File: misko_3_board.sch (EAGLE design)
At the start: 179 parts, among them IC1 ATMEGA1281-16AU, IC10 ORG1510-MK4, IC11 TPS3808G33DBVT, IC12 LTC4425, IC13 RN-42, IC14 ADXL345, IC15 74HCT1G32, IC16 FM25W256-SOIC, IC17 MICROSD_SPI_MODE, IC18 FH12-30S-0.5SH, IC19 DS1394U-33+, IC2 MC1525TT, IC20 115Q-BCA0, IC21 SIM800, IC3 TMP36GRTZ, IC4 TPS63031, IC5 MCP73871-2AAI/ML, IC6 SN74HCT14DR, IC7 FT230XS, IC8 SN74LVC1G3157DBVR - BT switch, IC9 SN74LVC1G3157DBVR - GPS switch, Q1 8MHz, Q2 LFXTAL016178R, T1 BSS84

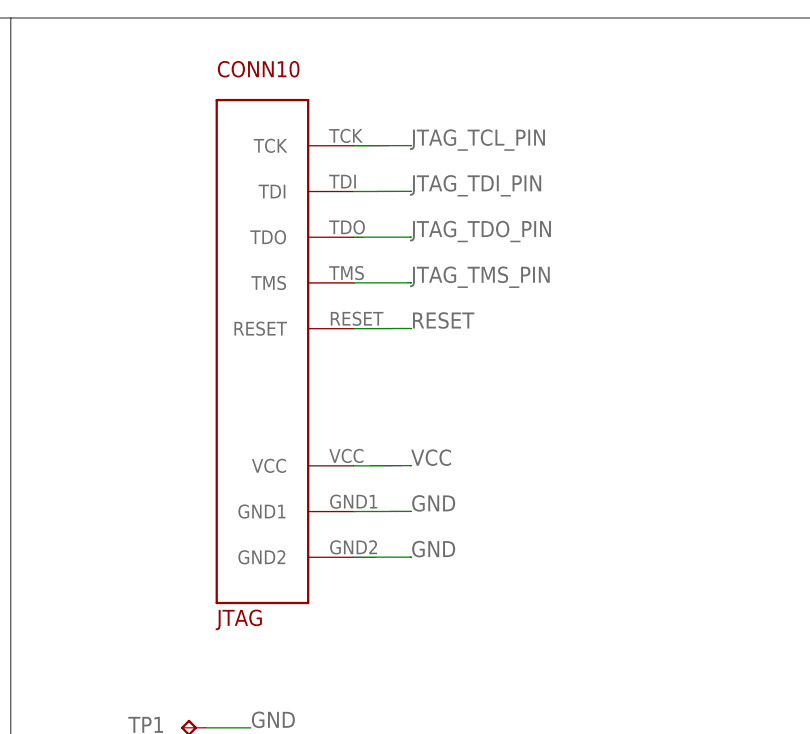
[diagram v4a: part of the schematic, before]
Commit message: - corrected for larger holes on 1.27mm connectors - moved fiducials around - rerouted a few traces around the 1.27mm connectors - added milling around mini usb socket
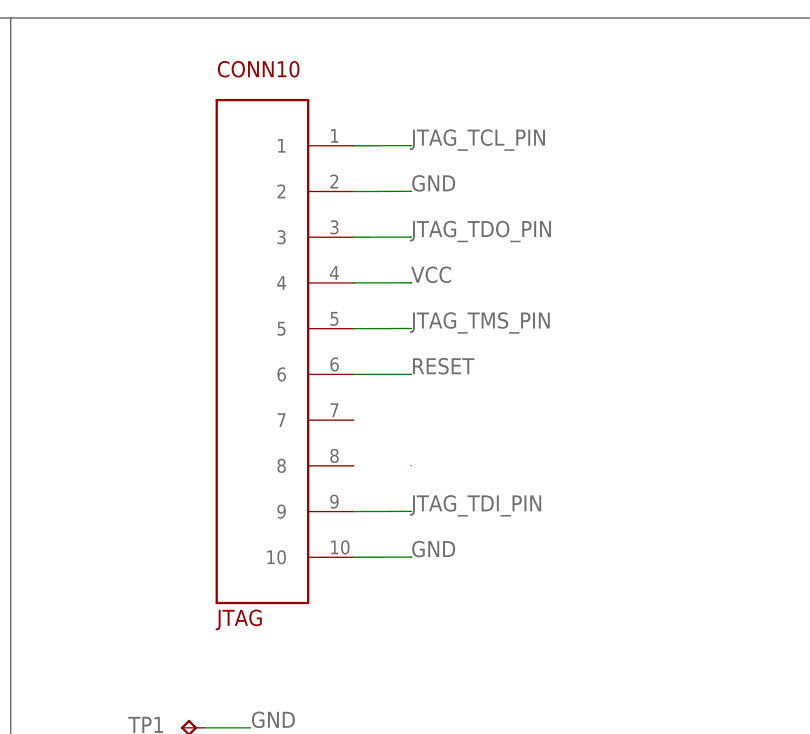
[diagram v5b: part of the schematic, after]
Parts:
- CONN10: device JTAG 1.27mm 10pin header:JTAG-1.27-10-PIN-HEADER -> 1.27mm 10pin header:1.27-10-PIN-HEADER
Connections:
- net GND: now also CONN10.10, CONN10.2; no longer CONN10.GND1, CONN10.GND2
- net JTAG_TCL_PIN: now also CONN10.1; no longer CONN10.TCK
- net JTAG_TDI_PIN: now also CONN10.9; no longer CONN10.TDI
- net JTAG_TDO_PIN: now also CONN10.3; no longer CONN10.TDO
- net JTAG_TMS_PIN: now also CONN10.5; no longer CONN10.TMS
- net RESET: now also CONN10.6; no longer CONN10.RESET
- net VCC: now also CONN10.4; no longer CONN10.VCC
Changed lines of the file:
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@@
 <setting verticaltext="up"/>
 </settings>
-<grid distance="0.1" unitdist="inch" unit="inch" style="lines" multiple="1" display="no" altdistance="0.01" altunitdist="inch" altunit="inch"/>
+<grid distance="1.27" unitdist="mm" unit="mm" style="lines" multiple="1" display="no" altdistance="0.01" altunitdist="inch" altunit="inch"/>
 <layers>
 <layer number="1" name="Top" color="4" fill="1" visible="no" active="no"/>
@@
 <part name="R54" library="rcl" deviceset="R-EU_" device="R0805" value="1k"/>
 <part name="C30" library="resistor" deviceset="C-EU" device="C0805" value="0.47µF"/>
-<part name="CONN10" library="JTAG 1.27mm 10pin header" deviceset="JTAG-1.27-10-PIN-HEADER" device="" value="JTAG"/>
+<part name="CONN10" library="1.27mm 10pin header" deviceset="1.27-10-PIN-HEADER" device="" value="JTAG"/>
 <part name="CONN12" library="1.27mm 10pin header" deviceset="1.27-10-PIN-HEADER" device="" value="board"/>
 <part name="CONN13" library="1.27mm 10pin header" deviceset="1.27-10-PIN-HEADER" device="" value="lid"/>
@@
 </segment>
 <segment>
-<pinref part="CONN10" gate="G$1" pin="VCC"/>
-<wire x1="278.13" y1="810.24" x2="284.48" y2="810.26" width="0.1524" layer="91"/>
 <wire x1="284.48" y1="810.24" x2="284.48" y2="810.26" width="0.1524" layer="91"/>
-<label x="284.48" y="810.26" size="1.778" layer="95" ratio="9"/>
 </segment>
 <segment>
@@
 <label x="213.36" y="76.2" size="1.778" layer="95"/>
 </segment>
+<segment>
+<pinref part="CONN10" gate="G$1" pin="4"/>
+<wire x1="278.13" y1="830.56" x2="284.48" y2="830.58" width="0.1524" layer="91"/>
+<wire x1="284.48" y1="830.56" x2="284.48" y2="830.58" width="0.1524" layer="91"/>
+<label x="284.48" y="830.58" size="1.778" layer="95" ratio="9"/>
+</segment>
 </net>
 <net name="GND" class="0">
@@
 </segment>
 <segment>
-<pinref part="CONN10" gate="G$1" pin="GND1"/>
-<wire x1="278.13" y1="805.16" x2="284.48" y2="805.18" width="0.1524" layer="91"/>
-<wire x1="284.48" y1="805.16" x2="284.48" y2="805.18" width="0.1524" layer="91"/>
-<label x="284.48" y="805.18" size="1.778" layer="95" ratio="9"/>
-</segment>
-<segment>
-<pinref part="CONN10" gate="G$1" pin="GND2"/>
+<pinref part="CONN10" gate="G$1" pin="10"/>
 <wire x1="278.13" y1="800.08" x2="284.48" y2="800.1" width="0.1524" layer="91"/>
 <wire x1="284.48" y1="800.08" x2="284.48" y2="800.1" width="0.1524" layer="91"/>
@@
 <pinref part="C47" gate="G$1" pin="-"/>
 </segment>
+<segment>
+<pinref part="CONN10" gate="G$1" pin="2"/>
+<wire x1="278.13" y1="840.72" x2="284.48" y2="840.74" width="0.1524" layer="91"/>
+<wire x1="284.48" y1="840.72" x2="284.48" y2="840.74" width="0.1524" layer="91"/>
+<label x="284.48" y="840.74" size="1.778" layer="95" ratio="9"/>
+</segment>
 </net>
 <net name="5V0" class="1">
@@
 </segment>
 <segment>
-<pinref part="CONN10" gate="G$1" pin="TDI"/>
-<wire x1="278.13" y1="840.72" x2="284.48" y2="840.74" width="0.1524" layer="91"/>
-<wire x1="284.48" y1="840.72" x2="284.48" y2="840.74" width="0.1524" layer="91"/>
-<label x="284.48" y="840.74" size="1.778" layer="95" ratio="9"/>
+<pinref part="CONN10" gate="G$1" pin="9"/>
+<wire x1="278.13" y1="805.16" x2="284.48" y2="805.18" width="0.1524" layer="91"/>
+<wire x1="284.48" y1="805.16" x2="284.48" y2="805.18" width="0.1524" layer="91"/>
+<label x="284.48" y="805.18" size="1.778" layer="95" ratio="9"/>
 </segment>
 </net>
@@
 </segment>
 <segment>
-<pinref part="CONN10" gate="G$1" pin="TDO"/>
+<pinref part="CONN10" gate="G$1" pin="3"/>
 <wire x1="278.13" y1="835.64" x2="284.48" y2="835.66" width="0.1524" layer="91"/>
 <wire x1="284.48" y1="835.64" x2="284.48" y2="835.66" width="0.1524" layer="91"/>
@@
 </segment>
 <segment>
-<pinref part="CONN10" gate="G$1" pin="TMS"/>
-<wire x1="278.13" y1="830.56" x2="284.48" y2="830.58" width="0.1524" layer="91"/>
-<wire x1="284.48" y1="830.56" x2="284.48" y2="830.58" width="0.1524" layer="91"/>
-<label x="284.48" y="830.58" size="1.778" layer="95" ratio="9"/>
+<pinref part="CONN10" gate="G$1" pin="5"/>
+<wire x1="278.13" y1="825.48" x2="284.48" y2="825.5" width="0.1524" layer="91"/>
+<wire x1="284.48" y1="825.48" x2="284.48" y2="825.5" width="0.1524" layer="91"/>
+<label x="284.48" y="825.5" size="1.778" layer="95" ratio="9"/>
 </segment>
 </net>
@@
 </segment>
 <segment>
-<pinref part="CONN10" gate="G$1" pin="TCK"/>
+<pinref part="CONN10" gate="G$1" pin="1"/>
 <wire x1="278.13" y1="845.8" x2="284.48" y2="845.82" width="0.1524" layer="91"/>
 <wire x1="284.48" y1="845.8" x2="284.48" y2="845.82" width="0.1524" layer="91"/>
@@
 </segment>
 <segment>
-<pinref part="CONN10" gate="G$1" pin="RESET"/>
-<wire x1="278.13" y1="825.48" x2="284.48" y2="825.5" width="0.1524" layer="91"/>
-<wire x1="284.48" y1="825.48" x2="284.48" y2="825.5" width="0.1524" layer="91"/>
-<label x="284.48" y="825.5" size="1.778" layer="95" ratio="9"/>
+<pinref part="CONN10" gate="G$1" pin="6"/>
+<wire x1="278.13" y1="820.4" x2="284.48" y2="820.4" width="0.1524" layer="91"/>
+<wire x1="284.48" y1="820.4" x2="284.48" y2="820.42" width="0.1524" layer="91"/>
+<label x="284.48" y="820.42" size="1.778" layer="95"/>
 </segment>
 </net>

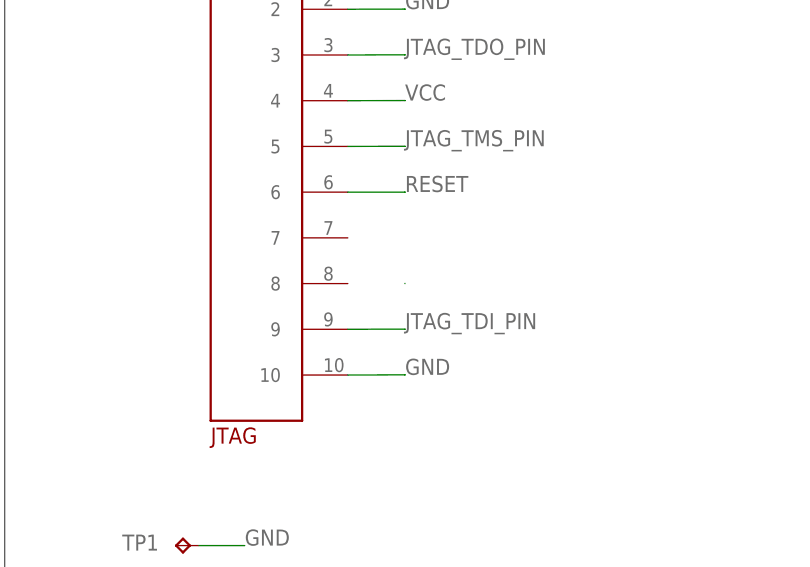
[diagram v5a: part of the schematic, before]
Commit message: - made wire-connected holes/traces larger
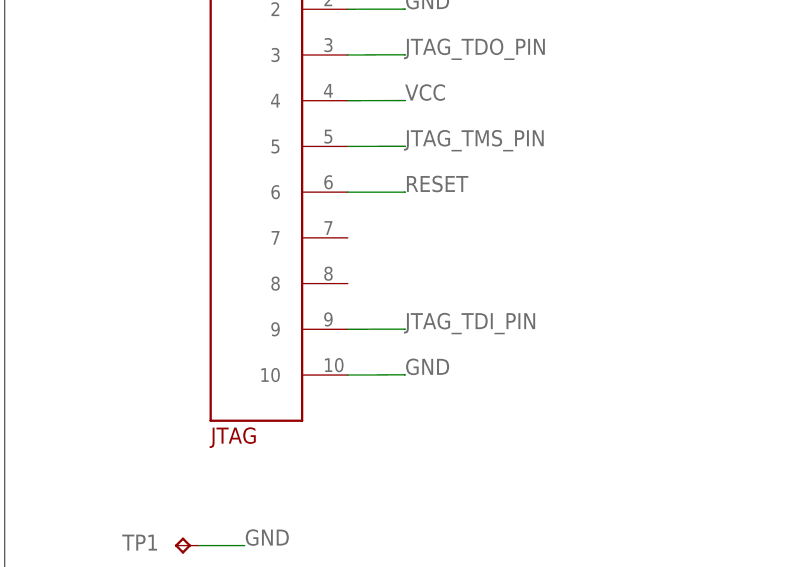
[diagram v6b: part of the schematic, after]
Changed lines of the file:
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@@
-</segment>
-<segment>
-<wire x1="284.48" y1="810.24" x2="284.48" y2="810.26" width="0.1524" layer="91"/>
 </segment>
 <segment>

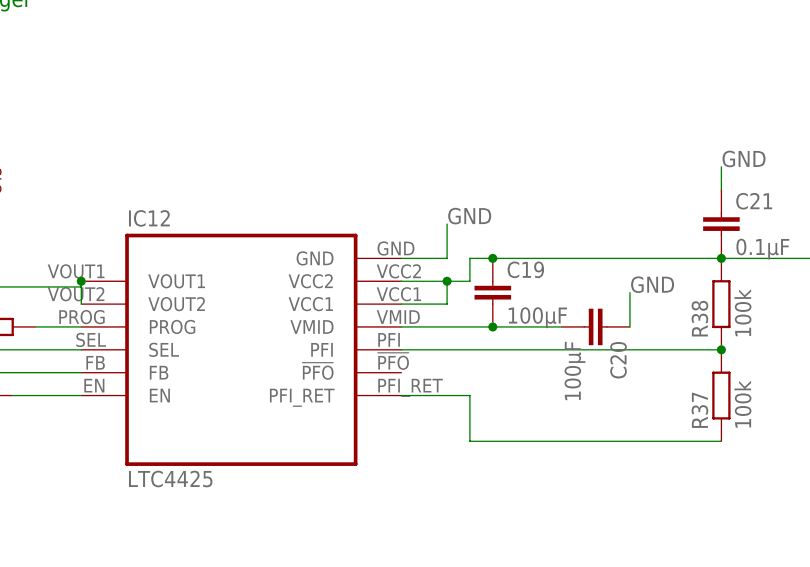
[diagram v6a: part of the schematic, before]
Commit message: - corrected wrong layout for ltc4425, updated gerber files
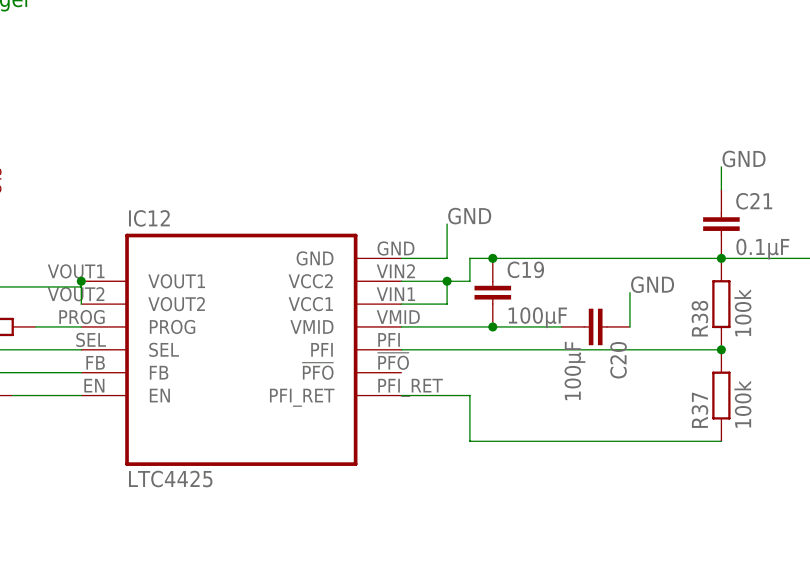
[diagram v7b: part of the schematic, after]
